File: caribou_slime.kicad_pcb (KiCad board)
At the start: 2 copper layers, 62.8 x 37.6 mm, 34 parts, among them J1 BATT JST, Q1 AO3145, U1 ESP32-C3_SUPERMINI, U2 BMI270, U3 FS312F-G, U4 FS8205A, U5 TP4056, U6 ME6211C33M5G

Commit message: fix(pcb): Clean up I2C lines
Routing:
- net SDA: track 54.3 -> 63.9 mm
- net SCL: track 35.7 -> 38.1 mm, vias 1 -> 0
- net GND: vias 44 -> 40
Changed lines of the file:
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@@
     )
   )
+  (gr_circle (center 50.546 54.61) (end 51.816 54.61)
+    (stroke (width 0.2) (type solid)) (fill solid) (layer "F.Cu"))
+  (gr_rect (start 49.572939 55.372) (end 51.816 56.896)
+    (stroke (width 0.2) (type solid)) (fill solid) (layer "F.Cu"))
+  (gr_rect (start 49.064939 54.61) (end 51.816 56.642)
+    (stroke (width 0.2) (type solid)) (fill solid) (layer "F.Cu"))
   (gr_line (start 34.43732 28.7655) (end 34.40176 28.58008)
     (stroke (width 0.1524) (type solid)) (layer "F.SilkS"))
@@
   (segment (start 55.805251 33.2365) (end 54.14425 33.2365) (width 0.25) (layer "F.Cu") (net 13))
   (via (at 58.46225 34.61) (size 0.8) (drill 0.4) (layers "F.Cu" "B.Cu") (net 13))
-  (via (at 51.054 57.658) (size 0.8) (drill 0.4) (layers "F.Cu" "B.Cu") (free) (net 13))
   (via (at 49.784 44.704) (size 0.8) (drill 0.4) (layers "F.Cu" "B.Cu") (free) (net 13))
   (via (at 52.578 46.482) (size 0.8) (drill 0.4) (layers "F.Cu" "B.Cu") (free) (net 13))
@@
   (via (at 35.814 34.29) (size 0.8) (drill 0.4) (layers "F.Cu" "B.Cu") (free) (net 13))
   (via (at 86.36 60.452) (size 0.8) (drill 0.4) (layers "F.Cu" "B.Cu") (free) (net 13))
-  (via (at 48.768 59.69) (size 0.8) (drill 0.4) (layers "F.Cu" "B.Cu") (free) (net 13))
   (via (at 49.784 46.482) (size 0.8) (drill 0.4) (layers "F.Cu" "B.Cu") (free) (net 13))
   (via (at 45.466 34.29) (size 0.8) (drill 0.4) (layers "F.Cu" "B.Cu") (free) (net 13))
-  (via (at 50.546 61.722) (size 0.8) (drill 0.4) (layers "F.Cu" "B.Cu") (free) (net 13))
   (via (at 72.39 60.452) (size 0.8) (drill 0.4) (layers "F.Cu" "B.Cu") (free) (net 13))
   (via (at 76.962 48.768) (size 0.8) (drill 0.4) (layers "F.Cu" "B.Cu") (free) (net 13))
@@
   (via (at 35.052 59.944) (size 0.8) (drill 0.4) (layers "F.Cu" "B.Cu") (free) (net 13))
   (via (at 35.052 48.514) (size 0.8) (drill 0.4) (layers "F.Cu" "B.Cu") (free) (net 13))
-  (via (at 50.8 54.356) (size 0.8) (drill 0.4) (layers "F.Cu" "B.Cu") (free) (net 13))
   (via (at 56.134 29.718) (size 0.8) (drill 0.4) (layers "F.Cu" "B.Cu") (free) (net 13))
   (via (at 39.624 59.944) (size 0.8) (drill 0.4) (layers "F.Cu" "B.Cu") (free) (net 13))
@@
   (segment (start 27.686 43.735) (end 31.322 43.735) (width 0.25) (layer "F.Cu") (net 21))
   (segment (start 31.322 43.735) (end 31.369 43.688) (width 0.25) (layer "F.Cu") (net 21))
-  (segment (start 56.772876 52.964429) (end 59.574 50.163305) (width 0.25) (layer "F.Cu") (net 22))
-  (segment (start 40.2665 62.7455) (end 47.2365 62.7455) (width 0.25) (layer "F.Cu") (net 22))
+  (segment (start 51.308 59.944) (end 50.292 60.96) (width 0.25) (layer "F.Cu") (net 22))
+  (segment (start 50.292 56.134) (end 51.308 57.15) (width 0.25) (layer "F.Cu") (net 22))
+  (segment (start 50.8 55.88) (end 51.816 54.864) (width 0.25) (layer "F.Cu") (net 22))
+  (segment (start 50.292 55.88) (end 50.8 55.88) (width 0.25) (layer "F.Cu") (net 22))
   (segment (start 54.825 42.164) (end 54.825 42.457) (width 0.25) (layer "F.Cu") (net 22))
+  (segment (start 49.53 55.88) (end 50.292 55.88) (width 0.25) (layer "F.Cu") (net 22))
+  (segment (start 48.7605 62.7455) (end 40.2665 62.7455) (width 0.25) (layer "F.Cu") (net 22))
+  (segment (start 51.308 57.15) (end 51.308 57.404) (width 0.25) (layer "F.Cu") (net 22))
   (segment (start 55.05 43.62) (end 54.61 43.18) (width 0.25) (layer "F.Cu") (net 22))
+  (segment (start 50.292 58.674) (end 51.308 59.69) (width 0.25) (layer "F.Cu") (net 22))
   (segment (start 54.825 42.457) (end 54.61 42.672) (width 0.25) (layer "F.Cu") (net 22))
-  (segment (start 54.394764 52.964429) (end 56.772876 52.964429) (width 0.25) (layer "F.Cu") (net 22))
-  (segment (start 59.574 50.163305) (end 59.574 45.096) (width 0.25) (layer "F.Cu") (net 22))
-  (segment (start 52.023943 55.33525) (end 54.394764 52.964429) (width 0.25) (layer "F.Cu") (net 22))
-  (segment (start 31.369 53.848) (end 40.2665 62.7455) (width 0.25) (layer "F.Cu") (net 22))
+  (segment (start 40.2665 62.7455) (end 31.369 53.848) (width 0.25) (layer "F.Cu") (net 22))
+  (segment (start 59.574 50.163305) (end 56.772876 52.964429) (width 0.25) (layer "F.Cu") (net 22))
   (segment (start 55.05 44.4885) (end 55.05 43.62) (width 0.25) (layer "F.Cu") (net 22))
-  (segment (start 59.574 45.096) (end 56.642 42.164) (width 0.25) (layer "F.Cu") (net 22))
+  (segment (start 50.292 58.42) (end 50.292 58.674) (width 0.25) (layer "F.Cu") (net 22))
+  (segment (start 56.642 42.164) (end 59.574 45.096) (width 0.25) (layer "F.Cu") (net 22))
+  (segment (start 50.292 60.96) (end 50.292 61.214) (width 0.25) (layer "F.Cu") (net 22))
   (segment (start 54.61 42.672) (end 54.61 43.18) (width 0.25) (layer "F.Cu") (net 22))
+  (segment (start 49.022 55.372) (end 49.53 55.88) (width 0.25) (layer "F.Cu") (net 22))
+  (segment (start 51.308 57.404) (end 50.292 58.42) (width 0.25) (layer "F.Cu") (net 22))
   (segment (start 54.61 43.18) (end 54.356 42.926) (width 0.25) (layer "F.Cu") (net 22))
-  (segment (start 47.2365 62.7455) (end 52.023943 57.958057) (width 0.25) (layer "F.Cu") (net 22))
-  (segment (start 52.023943 57.958057) (end 52.023943 55.33525) (width 0.25) (layer "F.Cu") (net 22))
+  (segment (start 51.816 53.594) (end 51.562 53.34) (width 0.25) (layer "F.Cu") (net 22))
+  (segment (start 56.772876 52.964429) (end 50.921571 52.964429) (width 0.25) (layer "F.Cu") (net 22))
+  (segment (start 50.921571 52.964429) (end 49.022 54.864) (width 0.25) (layer "F.Cu") (net 22))
   (segment (start 54.356 42.926) (end 53.086 42.926) (width 0.25) (layer "F.Cu") (net 22))
+  (segment (start 51.816 54.864) (end 51.816 53.594) (width 0.25) (layer "F.Cu") (net 22))
+  (segment (start 49.022 54.864) (end 49.022 55.372) (width 0.25) (layer "F.Cu") (net 22))
+  (segment (start 50.292 61.214) (end 48.7605 62.7455) (width 0.25) (layer "F.Cu") (net 22))
   (segment (start 54.61 42.672) (end 54.356 42.926) (width 0.25) (layer "F.Cu") (net 22))
+  (segment (start 50.292 55.88) (end 50.292 56.134) (width 0.25) (layer "F.Cu") (net 22))
+  (segment (start 51.308 59.69) (end 51.308 59.944) (width 0.25) (layer "F.Cu") (net 22))
+  (segment (start 59.574 45.096) (end 59.574 50.163305) (width 0.25) (layer "F.Cu") (net 22))
   (via (at 56.642 42.164) (size 0.8) (drill 0.4) (layers "F.Cu" "B.Cu") (net 22))
   (via (at 54.825 42.164) (size 0.8) (drill 0.4) (layers "F.Cu" "B.Cu") (net 22))
@@
   (segment (start 54.356 39.624) (end 53.086 39.624) (width 0.25) (layer "F.Cu") (net 23))
   (segment (start 55.55 44.4885) (end 55.55 43.18) (width 0.25) (layer "F.Cu") (net 23))
-  (segment (start 59.124 49.7311) (end 59.124 45.408) (width 0.25) (layer "F.Cu") (net 23))
+  (segment (start 55.88 42.926) (end 56.642 42.926) (width 0.25) (layer "F.Cu") (net 23))
   (segment (start 55.55 43.18) (end 55.55 42.926) (width 0.25) (layer "F.Cu") (net 23))
   (segment (start 55.804 42.926) (end 55.55 43.18) (width 0.25) (layer "F.Cu") (net 23))
-  (segment (start 56.7851 52.07) (end 59.124 49.7311) (width 0.25) (layer "F.Cu") (net 23))
   (segment (start 55.88 42.926) (end 55.804 42.926) (width 0.25) (layer "F.Cu") (net 23))
-  (segment (start 59.124 45.408) (end 56.642 42.926) (width 0.25) (layer "F.Cu") (net 23))
   (segment (start 55.55 42.926) (end 55.55 40.818) (width 0.25) (layer "F.Cu") (net 23))
+  (segment (start 56.7851 52.07) (end 48.514 52.07) (width 0.25) (layer "F.Cu") (net 23))
   (segment (start 55.804 42.926) (end 55.55 42.672) (width 0.25) (layer "F.Cu") (net 23))
   (segment (start 55.88 42.926) (end 55.55 42.926) (width 0.25) (layer "F.Cu") (net 23))
   (segment (start 55.55 40.818) (end 54.356 39.624) (width 0.25) (layer "F.Cu") (net 23))
-  (segment (start 56.642 42.926) (end 55.88 42.926) (width 0.25) (layer "F.Cu") (net 23))
-  (segment (start 56.642 52.07) (end 56.7851 52.07) (width 0.25) (layer "F.Cu") (net 23))
-  (via (at 56.642 52.07) (size 0.8) (drill 0.4) (layers "F.Cu" "B.Cu") (net 23))
-  (segment (start 50.292 57.067193) (end 55.289193 52.07) (width 0.25) (layer "B.Cu") (net 23))
-  (segment (start 49.276 61.468) (end 50.292 60.452) (width 0.25) (layer "B.Cu") (net 23))
-  (segment (start 50.292 60.452) (end 50.292 57.067193) (width 0.25) (layer "B.Cu") (net 23))
-  (segment (start 55.289193 52.07) (end 56.642 52.07) (width 0.25) (layer "B.Cu") (net 23))
-  (segment (start 46.609 61.468) (end 49.276 61.468) (width 0.25) (layer "B.Cu") (net 23))
+  (segment (start 48.514 52.07) (end 48.26 52.324) (width 0.25) (layer "F.Cu") (net 23))
+  (segment (start 56.642 42.926) (end 59.124 45.408) (width 0.25) (layer "F.Cu") (net 23))
+  (segment (start 48.26 59.817) (end 46.609 61.468) (width 0.25) (layer "F.Cu") (net 23))
+  (segment (start 48.26 52.324) (end 48.26 59.817) (width 0.25) (layer "F.Cu") (net 23))
+  (segment (start 59.124 45.408) (end 59.124 49.7311) (width 0.25) (layer "F.Cu") (net 23))
+  (segment (start 59.124 49.7311) (end 56.7851 52.07) (width 0.25) (layer "F.Cu") (net 23))
   (segment (start 70.2365 30.226) (end 68.570695 30.226) (width 0.25) (layer "F.Cu") (net 24))
   (segment (start 67.794 31.002695) (end 67.794 33.853) (width 0.25) (layer "F.Cu") (net 24))

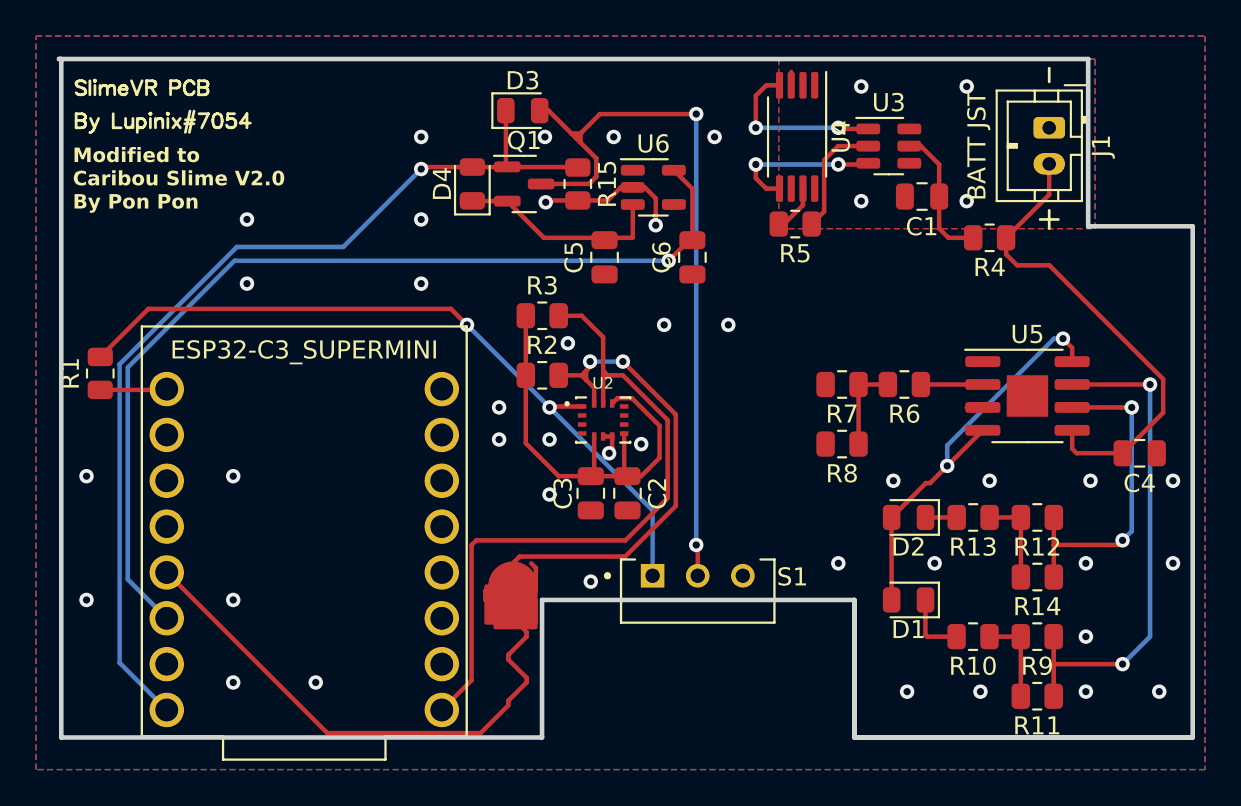
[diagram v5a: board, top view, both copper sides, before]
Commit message: fix(pcb): Resolve all DRC errors
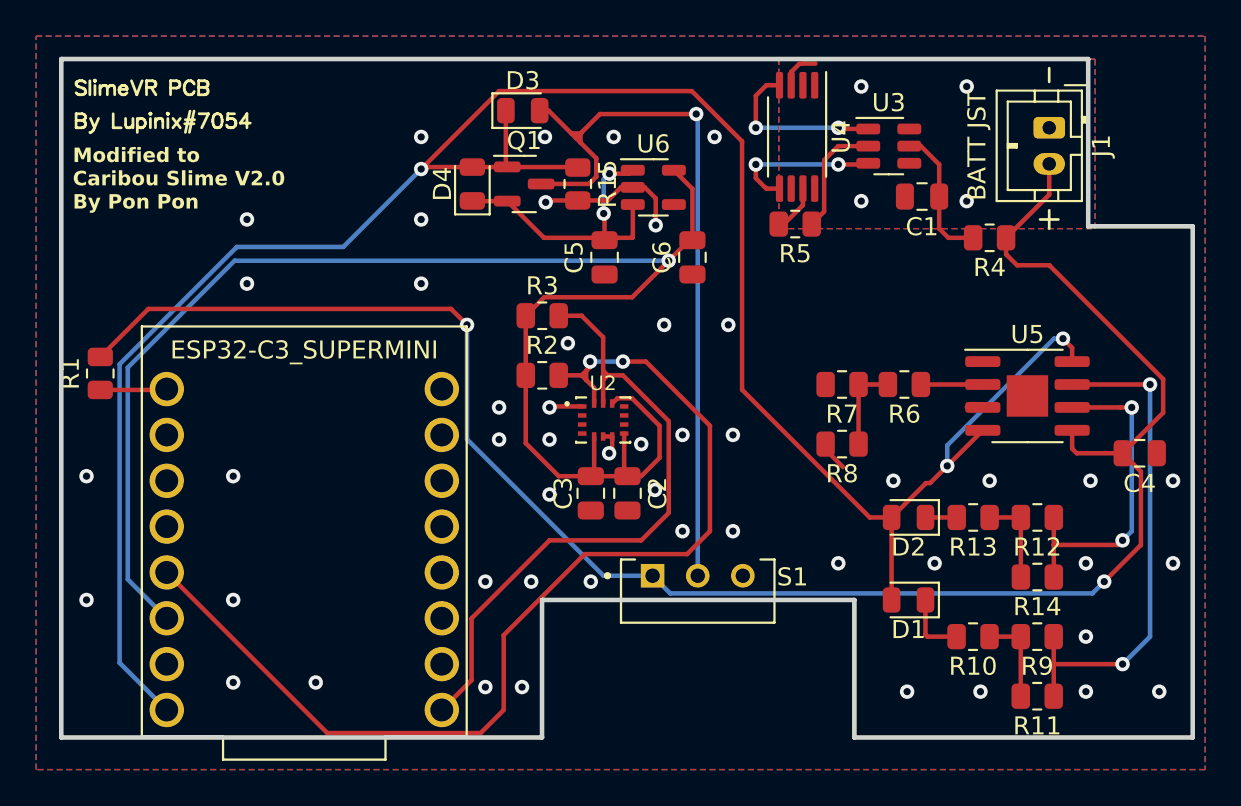
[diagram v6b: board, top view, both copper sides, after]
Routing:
- net +5V: track 76.4 -> 122.1 mm
- net VBAT: track 66.5 -> 102.1 mm, vias 1 -> 2
- net +3V3: track 78.8 -> 88.0 mm
- net Net-(D4-K): track 11.6 -> 16.8 mm, vias 0 -> 2
- net SDA: track 63.9 -> 59.4 mm
- net SCL: track 38.1 -> 36.3 mm
- net GND: track 15.1 -> 16.8 mm, vias 40 -> 49
- net Net-(J1-Pin_1): track 0.74 -> 2.27 mm
- net Net-(D3-A): vias 2 -> 1
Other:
- board size 62.8 x 37.6 mm -> 62.7 x 37.6 mm

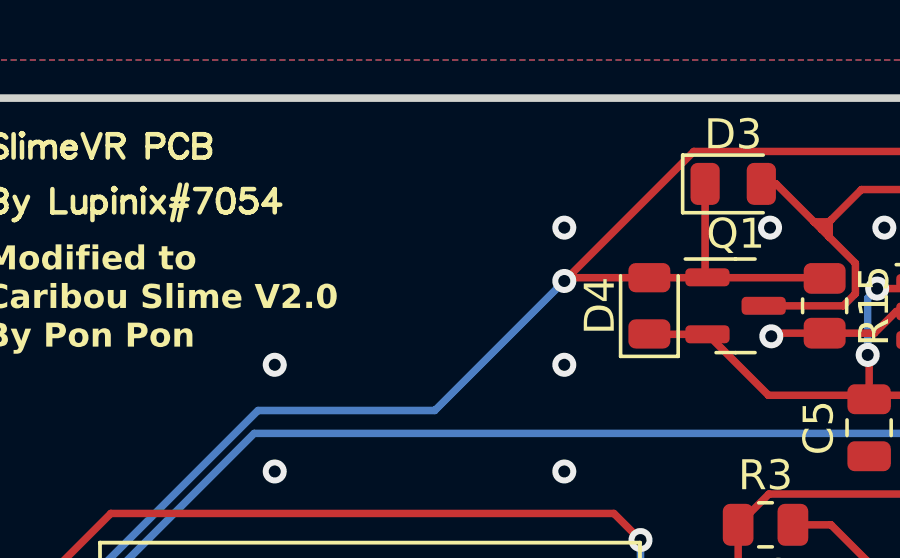
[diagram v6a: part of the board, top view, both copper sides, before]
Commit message: docs(pcb): Add QR code to repo on silk
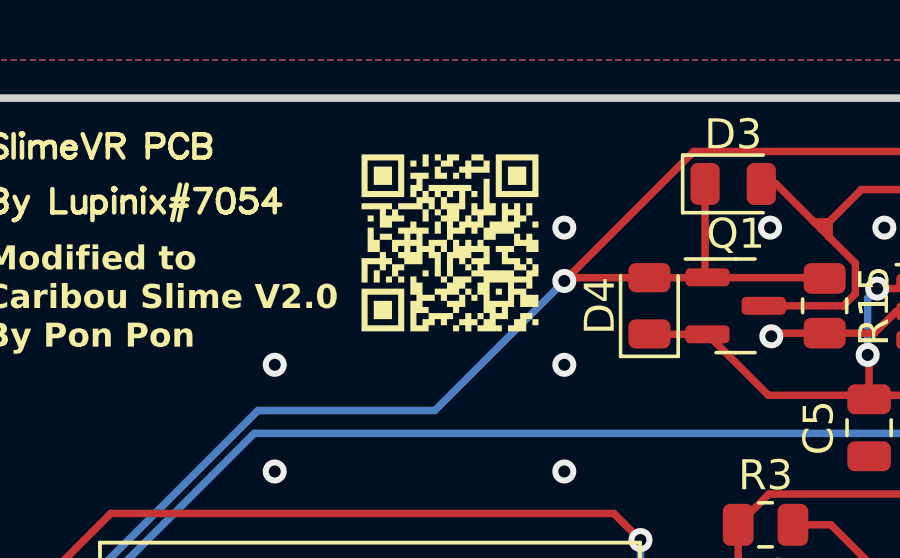
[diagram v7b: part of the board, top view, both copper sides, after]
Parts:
- added G***: LOGO, LOGO, F.Cu at (41.7, 30.2)

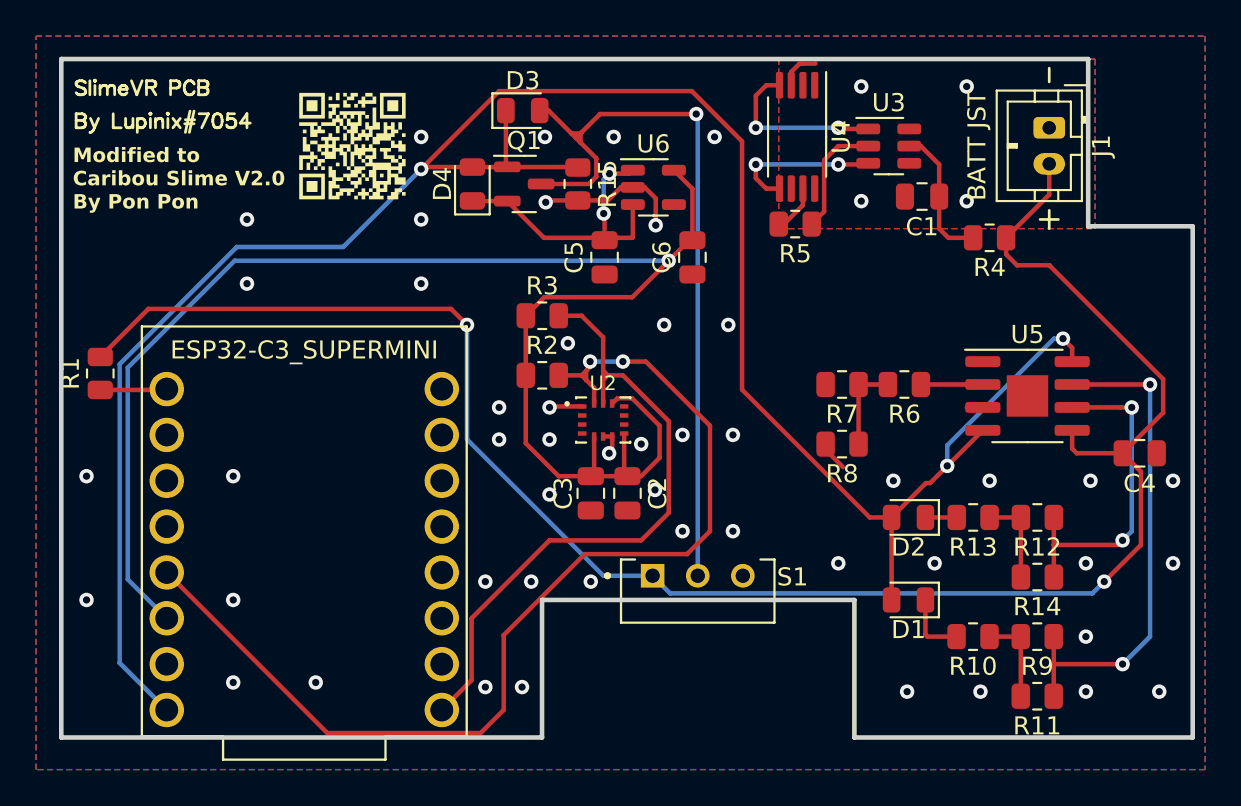
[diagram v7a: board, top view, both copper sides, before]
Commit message: fix(pcb): Correct battery sense voltage divider
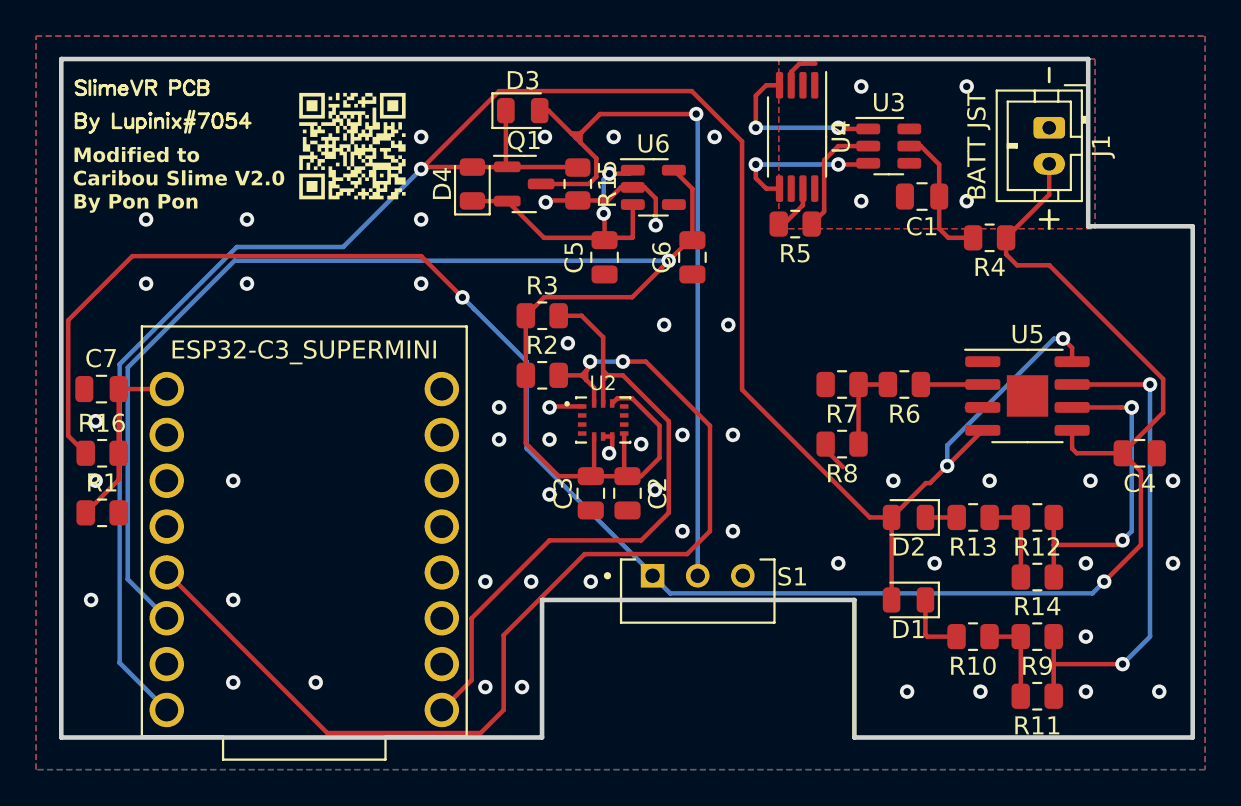
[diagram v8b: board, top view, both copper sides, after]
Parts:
- added C7: 100nF, Capacitor_SMD:C_0805_2012Metric, F.Cu at (27.8, 43.7)
- added R16: 220k, Resistor_SMD:R_0805_2012Metric, F.Cu at (27.8, 47.2)
- R1: value 180k -> 220k
- R15: value 180k -> 10k
- R4: value 100 -> 100R
- moved R1 7.72 mm to (27.8, 50.5), turned to 0 degrees
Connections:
- R1 pad 2: VBAT -> GND
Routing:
- net VBAT: track 102.1 -> 112.4 mm
- net Net-(U1-GPIO0): track 3.70 -> 10.3 mm
- net GND: vias 49 -> 52
